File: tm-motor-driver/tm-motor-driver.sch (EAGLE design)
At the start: 18 parts

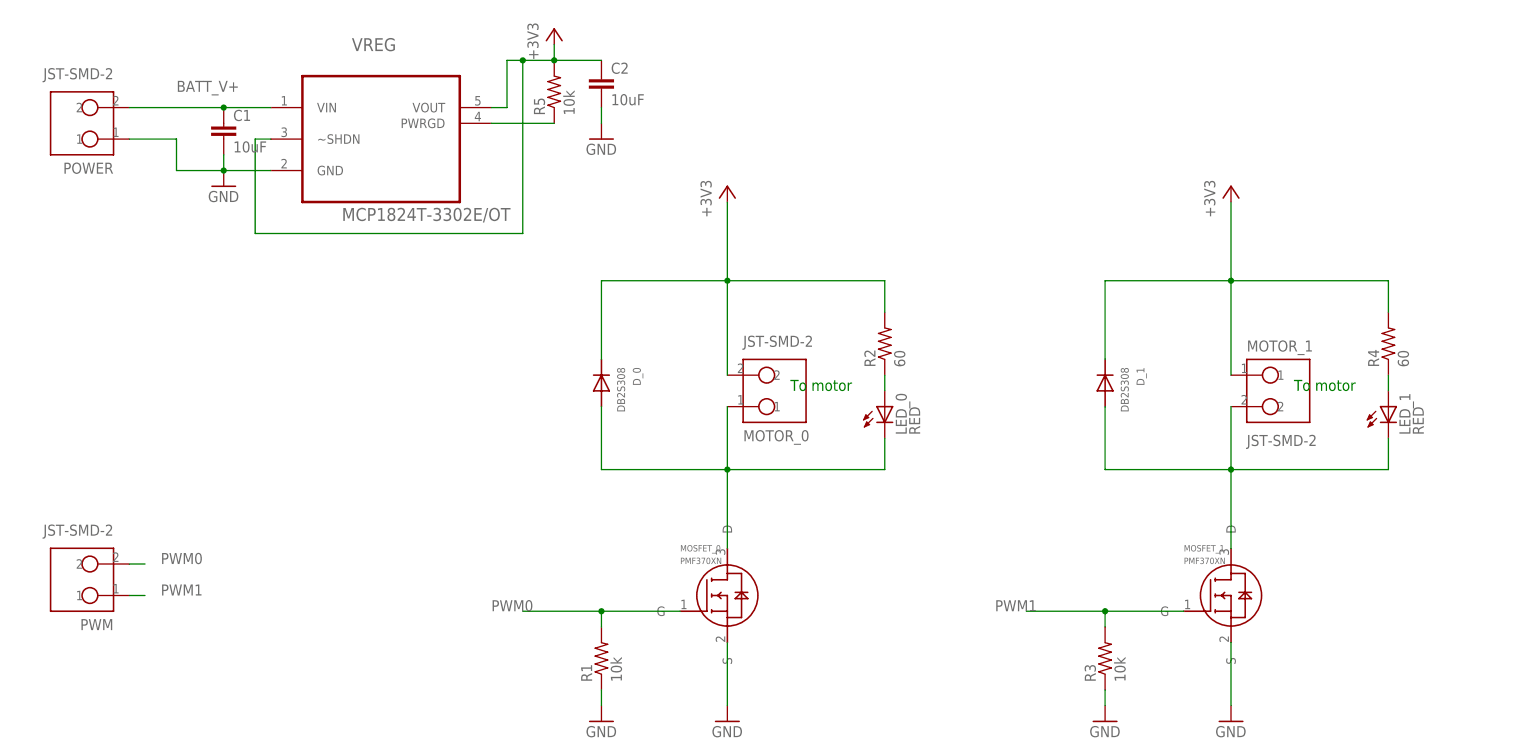
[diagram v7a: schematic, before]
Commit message: Replaced JST with picoblade
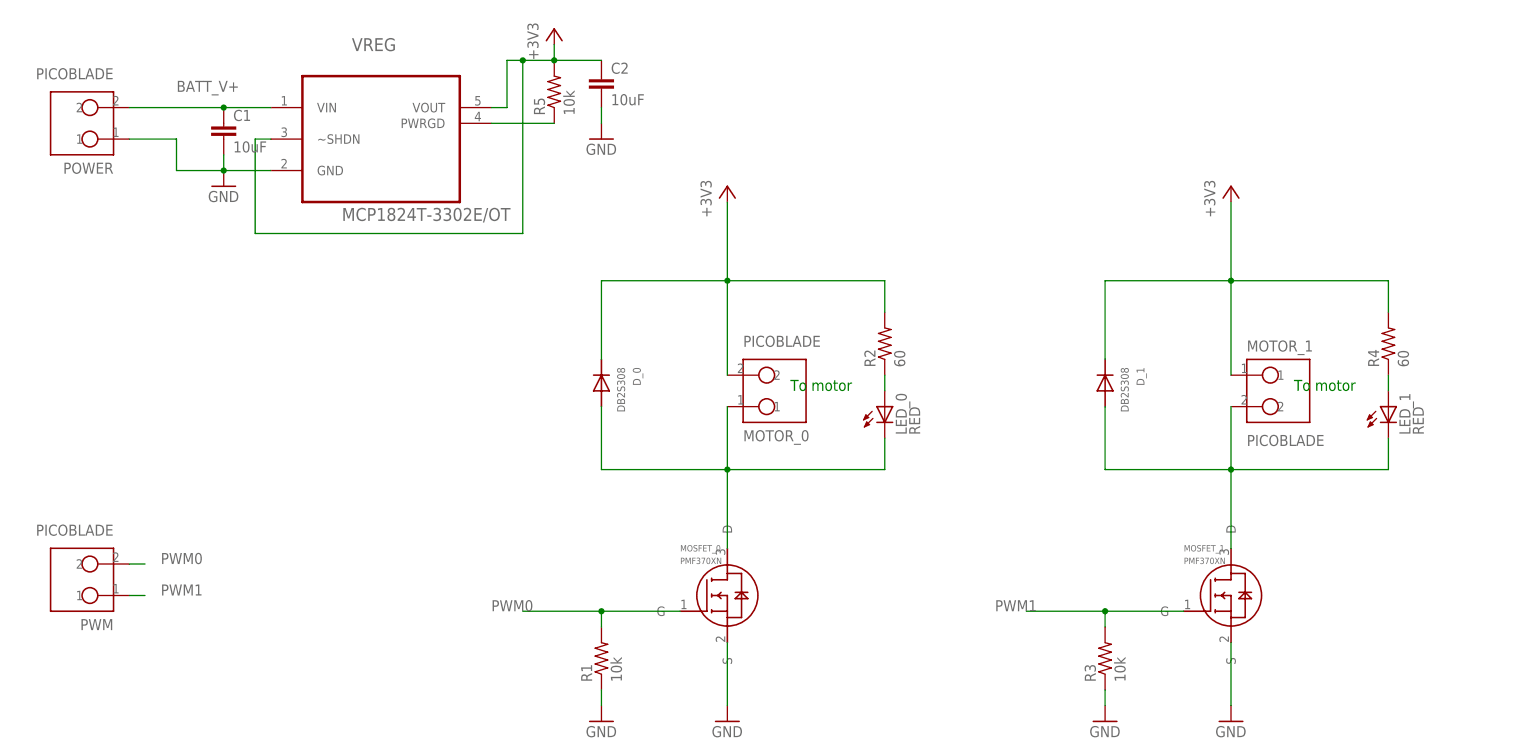
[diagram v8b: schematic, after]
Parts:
- MOTOR_0, MOTOR_1, POWER, PWM: value JST-SMD-2 -> PICOBLADE; device tactile-music:JST-SMD-2 -> tactile-music:PICOBLADE
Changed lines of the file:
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@@
 <part name="D_0" library="tactile-music" deviceset="DB2S308" device=""/>
 <part name="MOSFET_0" library="tactile-music" deviceset="PMF370XN" device=""/>
-<part name="MOTOR_0" library="tactile-music" deviceset="JST-SMD-2" device=""/>
+<part name="MOTOR_0" library="tactile-music" deviceset="PICOBLADE" device=""/>
 <part name="R1" library="resistor" deviceset="R-US_" device="R0805" value="10k"/>
 <part name="LED_0" library="led" deviceset="LED" device="CHIPLED_0805" value="RED"/>
@@
 <part name="D_1" library="tactile-music" deviceset="DB2S308" device=""/>
 <part name="MOSFET_1" library="tactile-music" deviceset="PMF370XN" device=""/>
-<part name="MOTOR_1" library="tactile-music" deviceset="JST-SMD-2" device=""/>
+<part name="MOTOR_1" library="tactile-music" deviceset="PICOBLADE" device=""/>
 <part name="R3" library="resistor" deviceset="R-US_" device="R0805" value="10k"/>
 <part name="LED_1" library="led" deviceset="LED" device="CHIPLED_0805" value="RED"/>
@@
 <part name="C2" library="rcl" deviceset="C-EU" device="C0805" value="10uF"/>
 <part name="R5" library="resistor" deviceset="R-US_" device="R0805" value="10k"/>
-<part name="POWER" library="tactile-music" deviceset="JST-SMD-2" device=""/>
-<part name="PWM" library="tactile-music" deviceset="JST-SMD-2" device=""/>
+<part name="POWER" library="tactile-music" deviceset="PICOBLADE" device=""/>
+<part name="PWM" library="tactile-music" deviceset="PICOBLADE" device=""/>
 </parts>
 <sheets>
